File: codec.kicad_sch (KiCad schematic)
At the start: 25 parts, among them J10 FCR684204T, J11 DIN_DOUT_2TP, J13 AJ_TP5, J14 C_G0, J15 C_G7, J16 C_RST, J17 C_CLKOUT, U4 WM8805GEDS_V, Y2 12M

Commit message: printed pdf from schematics
Signed-off-by: Mika Laitio <lamikr@gmail.com>
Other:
- company: (none) -> Mika Laitio
- title: (none) -> I2S Audio to AES/EBU Optical Toslink
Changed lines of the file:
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@@
   (paper "A4")
   (title_block
+    (title "I2S Audio to AES/EBU Optical Toslink")
     (date "2023-12-26")
     (rev "v0.1")
+    (company "Mika Laitio")
   )
   (junction (at 235.966 138.176) (diameter 0) (color 0 0 0 0)

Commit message: added mpn and sku_digikey numbers for bom
Signed-off-by: Mika Laitio <lamikr@gmail.com>
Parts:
- C17, C18: MFR (none) -> Murata; MPN (none) -> GJM1555C1H160GB01D; SKU_DIGIKEY (none) -> 490-8081-1-ND
- C19, C20: MFR (none) -> Murata; MPN (none) -> GRM033R61A104ME15D; SKU_DIGIKEY (none) -> 490-5405-1-ND
- C21: value C -> 0u1F; MFR (none) -> Murata; MPN (none) -> GRM033R61A104ME15D; SKU_DIGIKEY (none) -> 490-5405-1-ND; now not fitted
- C22, C23: MFR (none) -> Murata; MPN (none) -> GCJ188R71H104KA12D; Price (none) -> 0.16; SKU_DIGIKEY (none) -> 490-5798-1-ND
- J10: Height 5.2 -> (none); MFR (none) -> CLIFF ELECTRONIC COMPONENTS; MPN (none) -> FCR684204T; Manufacturer_Name CLIFF ELECTRONIC COMPONENTS -> (none); Manufacturer_Part_Number FCR684204T -> (none); Price (none) -> 4.22; SKU_DIGIKEY (none) -> 4654-FCR684204T-ND
- J11: MFR (none) -> Adam Tech; MPN (none) -> HPH1-A-20-UA; Notes (none) -> 1x20 pin header; Price (none) -> 0.72; SKU_DIGIKEY (none) -> 2057-HPH1-A-20-UA-ND
- J13: MFR (none) -> Sullins Connector Solutions; MPN (none) -> S9014E-05-ND; Price (none) -> 0.40; SKU_DIGIKEY (none) -> GRPB051VWVN-RC
- R10, R11: MFR (none) -> Yageo; MPN (none) -> RC0603JR-070RL; Price (none) -> 0.1; SKU_DIGIKEY (none) -> 311-0.0GRCT-ND
- R12: MFR (none) -> Yageo; MPN (none) -> RC0603JR-07110RL; Price (none) -> 0.1; SKU_DIGIKEY (none) -> 311-110GRCT-ND
- R13: MFR (none) -> Yageo; MPN (none) -> RC0603FR-07210RL; Price (none) -> 0.1; SKU_DIGIKEY (none) -> 311-210HRCT-ND
- R6, R7, R8, R9: MFR (none) -> Yageo; MPN (none) -> RC0402FR-0710KL; Price (none) -> 0.1; SKU_DIGIKEY (none) -> 311-10.0KLRCT-ND
- U4: MFR (none) -> Cirrus Logic; MPN (none) -> WM8805GEDS_V; Price (none) -> 12; SKU_DIGIKEY (none) -> 598-2396-ND
- Y2: MFR (none) -> Abracon LLC; MPN (none) -> ABM7-12.000MHZ-D2Y-T; Price (none) -> 0.67; SKU_DIGIKEY (none) -> 535-9836-1-ND; sku_digikey 535-9836-1-ND -> (none)

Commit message: optimized bom from digikey
Signed-off-by: Mika Laitio <lamikr@gmail.com>
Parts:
- C17, C18, C19, C20, C21, C22, C23, R10, R11, R12, R13, R6, R7, R8, R9: QtyOrdered (none) -> 100
- J10, U4: QtyOrdered (none) -> 3
- J11, J13, Y2: QtyOrdered (none) -> 10
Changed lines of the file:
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@@
+      (effects (font (size 1.27 1.27)) hide)
+    )
+    (property "QtyOrdered" "100" (at 64.008 74.676 0)
       (effects (font (size 1.27 1.27)) hide)
     )
@@
     )
     (property "SKU_DIGIKEY" "311-10.0KLRCT-ND" (at 58.928 55.626 0)
+      (effects (font (size 1.27 1.27)) hide)
+    )
+    (property "QtyOrdered" "100" (at 58.928 55.626 0)
       (effects (font (size 1.27 1.27)) hide)
     )
@@
       (effects (font (size 1.27 1.27)) hide)
     )
+    (property "QtyOrdered" "100" (at 130.048 162.56 0)
+      (effects (font (size 1.27 1.27)) hide)
+    )
     (pin "1")
     (pin "2")
@@
       (effects (font (size 1.27 1.27)) hide)
     )
+    (property "QtyOrdered" "100" (at 107.188 173.99 0)
+      (effects (font (size 1.27 1.27)) hide)
+    )
     (pin "2")
     (pin "1")
@@
       (effects (font (size 1.27 1.27)) hide)
     )
+    (property "QtyOrdered" "100" (at 116.078 154.94 0)
+      (effects (font (size 1.27 1.27)) hide)
+    )
     (pin "2")
     (pin "1")
@@
     )
     (property "Price" "" (at 222.504 48.006 0)
+      (effects (font (size 1.27 1.27)) hide)
+    )
+    (property "QtyOrdered" "" (at 222.504 48.006 0)
       (effects (font (size 1.27 1.27)) hide)
     )
@@
       (effects (font (size 1.27 1.27)) hide)
     )
+    (property "QtyOrdered" "10" (at 157.988 70.866 0)
+      (effects (font (size 1.27 1.27)) hide)
+    )
     (pin "2")
     (pin "1")
@@
     )
     (property "SKU_DIGIKEY" "490-8081-1-ND" (at 247.396 138.176 0)
+      (effects (font (size 1.27 1.27)) hide)
+    )
+    (property "QtyOrdered" "100" (at 247.396 138.176 0)
       (effects (font (size 1.27 1.27)) hide)
     )
@@
       (effects (font (size 1.27 1.27)) hide)
     )
+    (property "QtyOrdered" "100" (at 181.61 115.57 0)
+      (effects (font (size 1.27 1.27)) hide)
+    )
     (pin "1")
     (pin "2")
@@
     )
     (property "SKU_DIGIKEY" "GRPB051VWVN-RC" (at 22.098 149.86 0)
+      (effects (font (size 1.27 1.27)) hide)
+    )
+    (property "QtyOrdered" "10" (at 22.098 149.86 0)
       (effects (font (size 1.27 1.27)) hide)
     )
@@
     )
     (property "SKU_DIGIKEY" "598-2396-ND" (at 67.818 35.306 0)
+      (effects (font (size 1.27 1.27)) hide)
+    )
+    (property "QtyOrdered" "3" (at 67.818 35.306 0)
       (effects (font (size 1.27 1.27)) hide)
     )
@@
       (effects (font (size 1.27 1.27)) hide)
     )
+    (property "QtyOrdered" "100" (at 65.278 28.956 0)
+      (effects (font (size 1.27 1.27)) hide)
+    )
     (pin "1")
     (pin "2")
@@
       (effects (font (size 1.27 1.27)) hide)
     )
+    (property "QtyOrdered" "100" (at 124.968 173.99 0)
+      (effects (font (size 1.27 1.27)) hide)
+    )
     (pin "2")
     (pin "1")
@@
     )
     (property "Price" "" (at 238.76 100.33 0)
+      (effects (font (size 1.27 1.27)) hide)
+    )
+    (property "QtyOrdered" "" (at 238.76 100.33 0)
       (effects (font (size 1.27 1.27)) hide)
     )
@@
       (effects (font (size 1.27 1.27)) hide)
     )
+    (property "QtyOrdered" "10" (at 235.966 144.526 0)
+      (effects (font (size 1.27 1.27)) hide)
+    )
     (pin "1")
     (pin "2")
@@
     )
     (property "SKU_DIGIKEY" "490-8081-1-ND" (at 247.396 150.876 0)
+      (effects (font (size 1.27 1.27)) hide)
+    )
+    (property "QtyOrdered" "100" (at 247.396 150.876 0)
       (effects (font (size 1.27 1.27)) hide)
     )
@@
       (effects (font (size 1.27 1.27)) hide)
     )
+    (property "QtyOrdered" "100" (at 96.52 118.11 0)
+      (effects (font (size 1.27 1.27)) hide)
+    )
     (pin "1")
     (pin "2")
@@
       (effects (font (size 1.27 1.27)) hide)
     )
+    (property "QtyOrdered" "100" (at 91.948 165.1 0)
+      (effects (font (size 1.27 1.27)) hide)
+    )
     (pin "2")
     (pin "1")
@@
       (effects (font (size 1.27 1.27)) hide)
     )
+    (property "QtyOrdered" "" (at 173.99 110.49 0)
+      (effects (font (size 1.27 1.27)) hide)
+    )
     (pin "1")
     (instances
@@
     )
     (property "Price" "" (at 88.9 113.03 0)
+      (effects (font (size 1.27 1.27)) hide)
+    )
+    (property "QtyOrdered" "" (at 88.9 113.03 0)
       (effects (font (size 1.27 1.27)) hide)
     )
@@
     )
     (property "SKU_DIGIKEY" "4654-FCR684204T-ND" (at 38.608 147.32 0)
+      (effects (font (size 1.27 1.27)) hide)
+    )
+    (property "QtyOrdered" "3" (at 38.608 147.32 0)
       (effects (font (size 1.27 1.27)) hide)
     )
@@
       (effects (font (size 1.27 1.27)) hide)
     )
+    (property "QtyOrdered" "100" (at 102.108 162.56 0)
+      (effects (font (size 1.27 1.27)) hide)
+    )
     (pin "2")
     (pin "1")
@@
       (effects (font (size 1.27 1.27)) hide)
     )
+    (property "QtyOrdered" "100" (at 116.078 168.91 0)
+      (effects (font (size 1.27 1.27)) hide)
+    )
     (pin "2")
     (pin "1")
@@
     )
     (property "Price" "" (at 41.91 113.03 0)
+      (effects (font (size 1.27 1.27)) hide)
+    )
+    (property "QtyOrdered" "" (at 41.91 113.03 0)
       (effects (font (size 1.27 1.27)) hide)
     )
@@
       (effects (font (size 1.27 1.27)) hide)
     )
+    (property "QtyOrdered" "100" (at 49.53 118.11 0)
+      (effects (font (size 1.27 1.27)) hide)
+    )

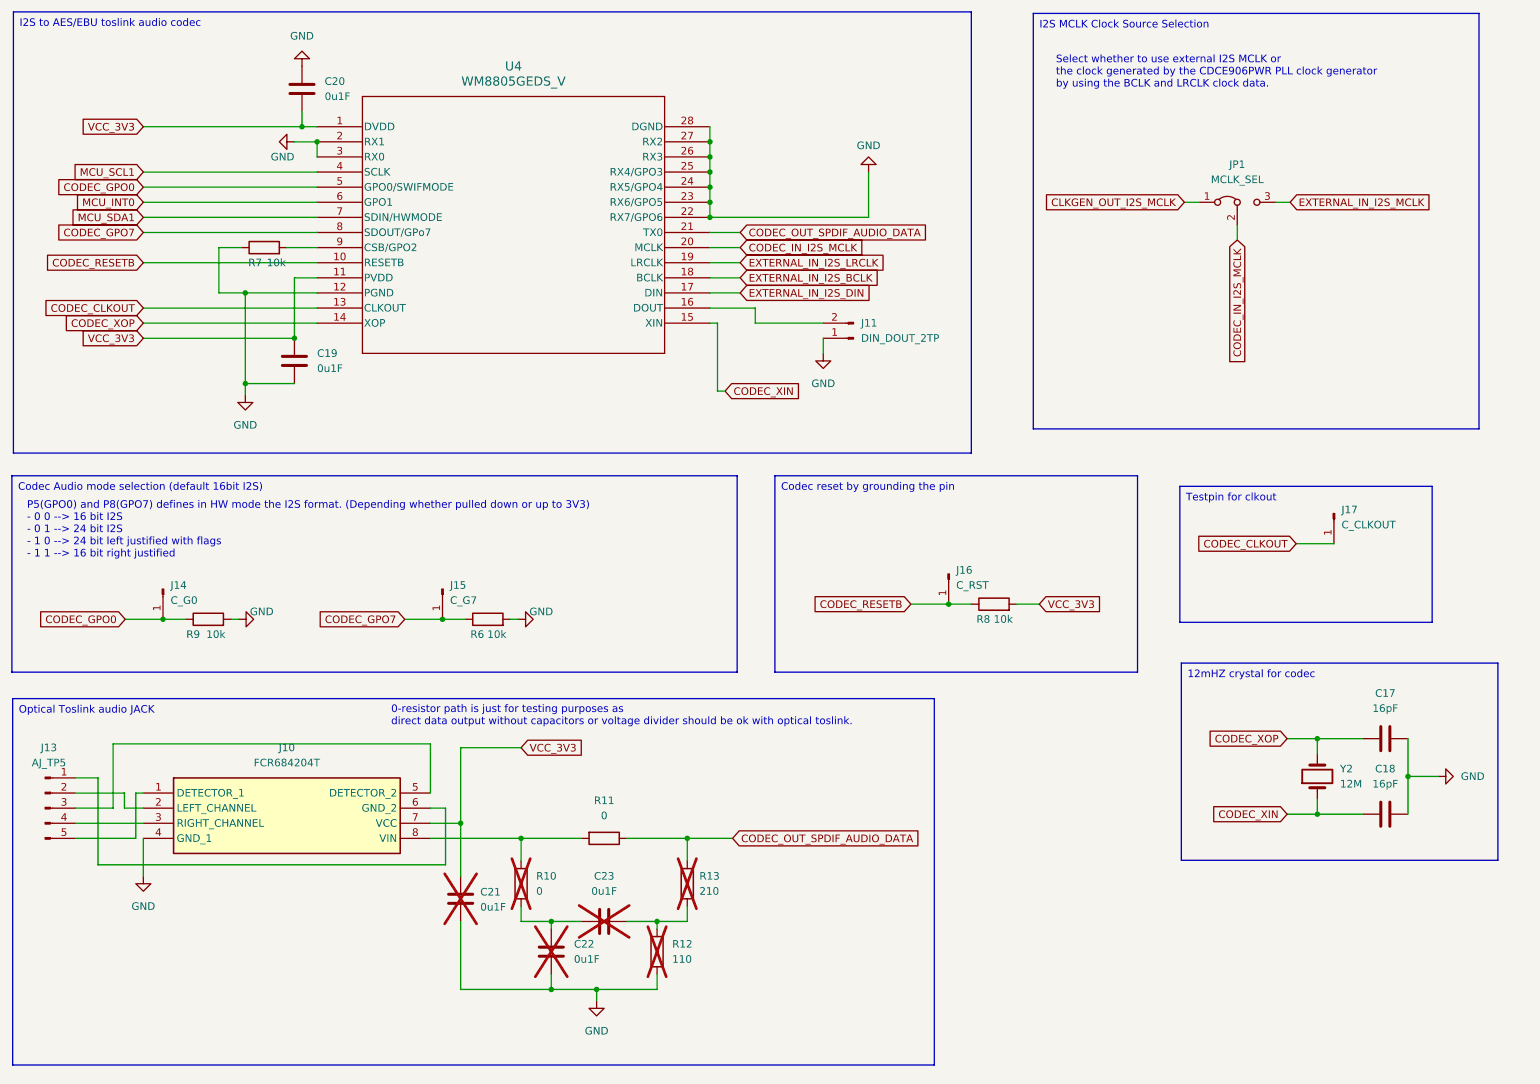
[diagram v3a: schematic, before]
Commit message: various updates
- removed duplicates 5V power connectors
- now the whole pcb is always powered via 6 pin
  atmega avr isp connector
- added connector for wm8805 rx0 and rx1
- added labels for jumpers/connectors
- moved the orientation of existing connecors
- moved the location of ldo close to
  6 pin avr isp connector

Signed-off-by: Mika Laitio <lamikr@gmail.com>
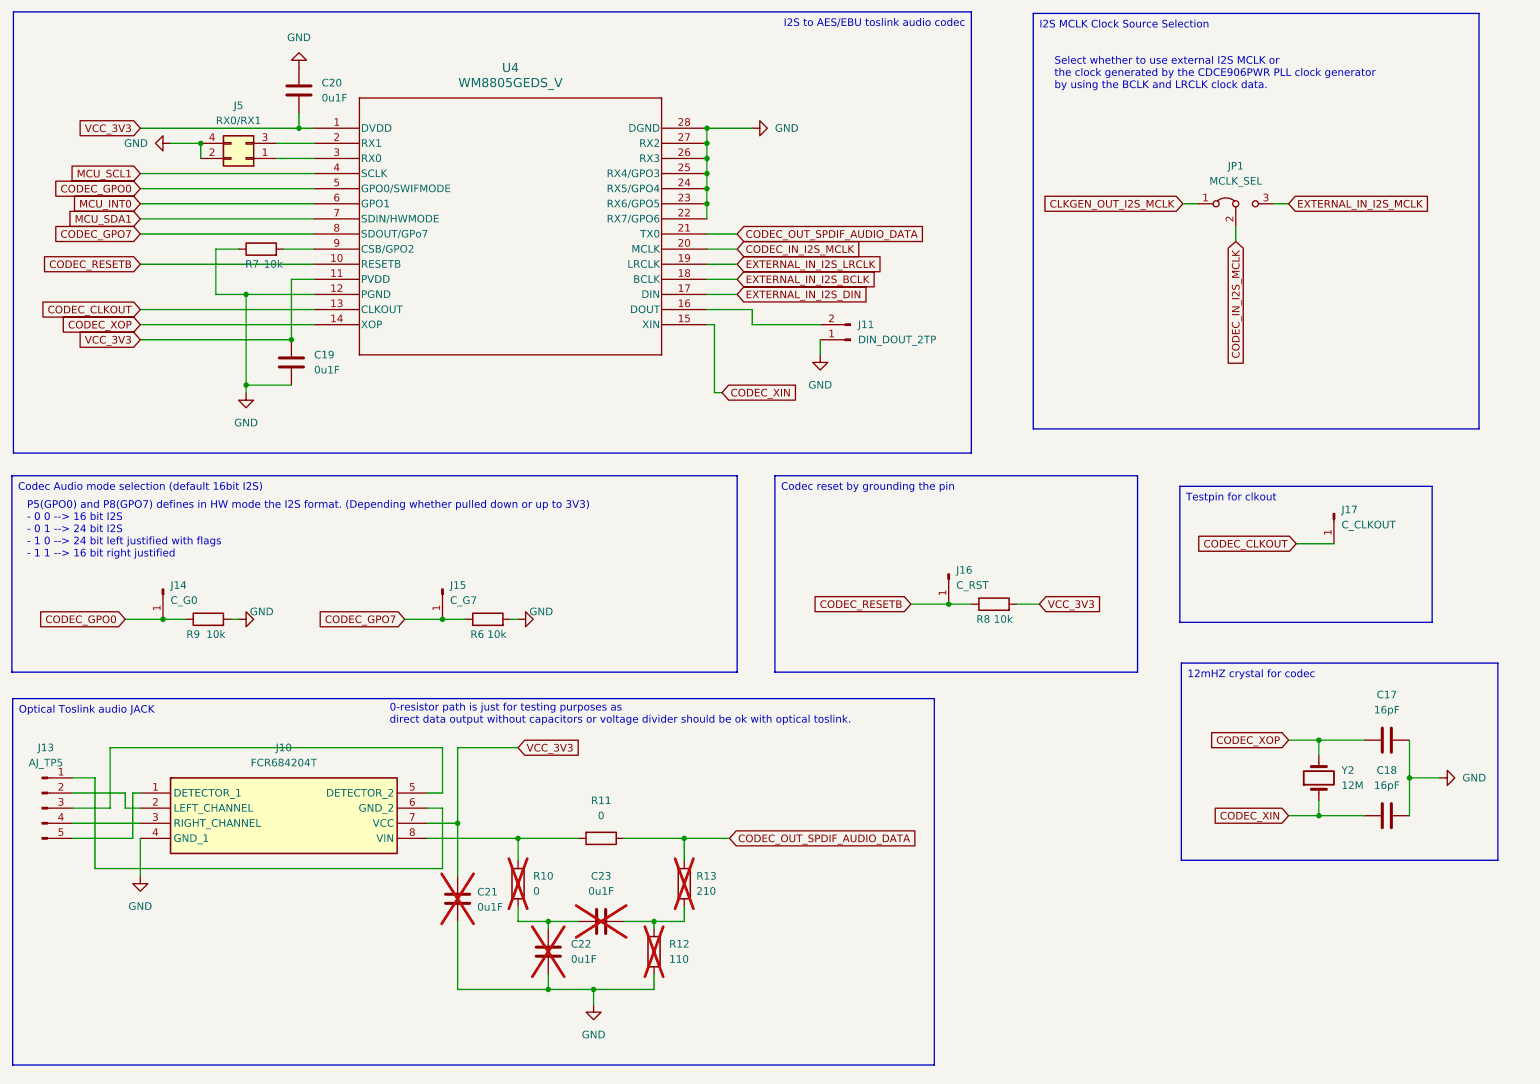
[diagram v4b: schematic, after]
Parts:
- added J5: RX0/RX1, Connector_PinHeader_2.54mm:PinHeader_2x02_P2.54mm_Vertical, symbol Connector_Generic:Conn_02x02_Odd_Even
- J10: footprint FCR684204T -> lamikr_audio:FCR684204T; Height (none) -> 5.2; Manufacturer_Name (none) -> CLIFF ELECTRONIC COMPONENTS; Manufacturer_Part_Number (none) -> FCR684204T
- U4: footprint SSOP28_WM8805GEDS_V_CIR -> lamikr_audio:SSOP28_WM8805GEDS_V_CIR
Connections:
- net GND: now also J5.2 (Pin_2), J5.4 (Pin_4); no longer U4.2 (RX1), U4.3 (RX0)
- new net: J5.3 (Pin_3), U4.2 (RX1)
- new net: J5.1 (Pin_1), U4.3 (RX0)
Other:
- moved on the sheet: C19, C20, C21, C22, C23, J10, J11, J13, R10, R11, R12, R13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

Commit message: finished v0.2 design
- mcu ftdi serial connector reset pin
  to 3v3 instead of 5v
- 3.3v pull-up resistor, cap and diode for mcu reset
- mcu reset button
- solder paste clearance -20% for
  mcu, codec, clk gen and ldo to help
  spreading pasta to small pins close to
  ech others

Signed-off-by: Mika Laitio <lamikr@gmail.com>
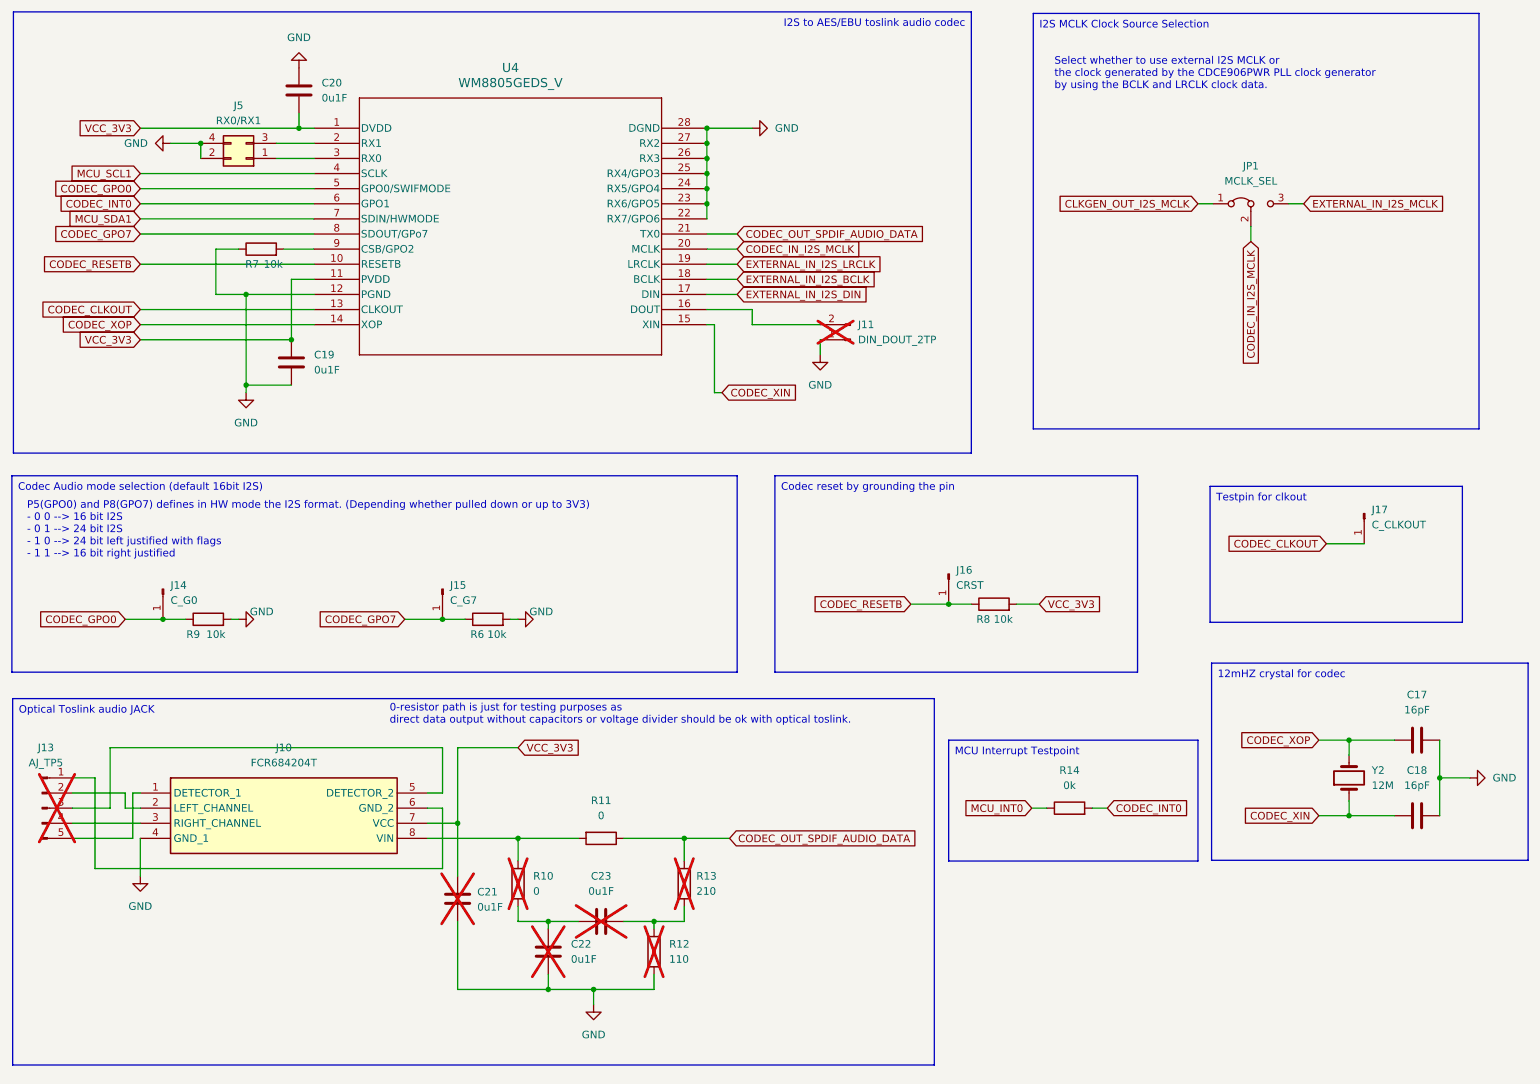
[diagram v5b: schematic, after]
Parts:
- added R14: 0k, Resistor_SMD:R_0402_1005Metric, symbol Device:R
- J11, J13: now not fitted
- J16: value C_RST -> CRST
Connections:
- net MCU_INT0: now also R14.1; no longer U4.6 (GPO1)
- new net CODEC_INT0: R14.2, U4.6 (GPO1)
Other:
- moved on the sheet: C17, C18, J17, JP1, Y2

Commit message: inceased the size of some tp headers to 2.00mm
Signed-off-by: Mika Laitio <lamikr@gmail.com>
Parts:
- J11: footprint Connector_PinHeader_1.27mm:PinHeader_1x02_P1.27mm_Vertical -> Connector_PinHeader_2.00mm:PinHeader_1x02_P2.00mm_Vertical
- J13: footprint Connector_PinHeader_1.27mm:PinHeader_1x05_P1.27mm_Vertical -> Connector_PinHeader_2.00mm:PinHeader_1x05_P2.00mm_Vertical
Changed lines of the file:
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@@
 			)
 		)
-		(property "Footprint" "Connector_PinHeader_1.27mm:PinHeader_1x02_P1.27mm_Vertical"
+		(property "Footprint" "Connector_PinHeader_2.00mm:PinHeader_1x02_P2.00mm_Vertical"
 			(at 157.48 71.12 0)
 			(effects
@@
 			)
 		)
-		(property "Footprint" "Connector_PinHeader_1.27mm:PinHeader_1x05_P1.27mm_Vertical"
+		(property "Footprint" "Connector_PinHeader_2.00mm:PinHeader_1x05_P2.00mm_Vertical"
 			(at 21.59 149.86 0)
 			(effects
